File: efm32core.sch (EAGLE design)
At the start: 57 parts, among them U2 HM-10, U3 USD-SOCKETNEW, X1 48.0MHz, Y1 32.768kHz

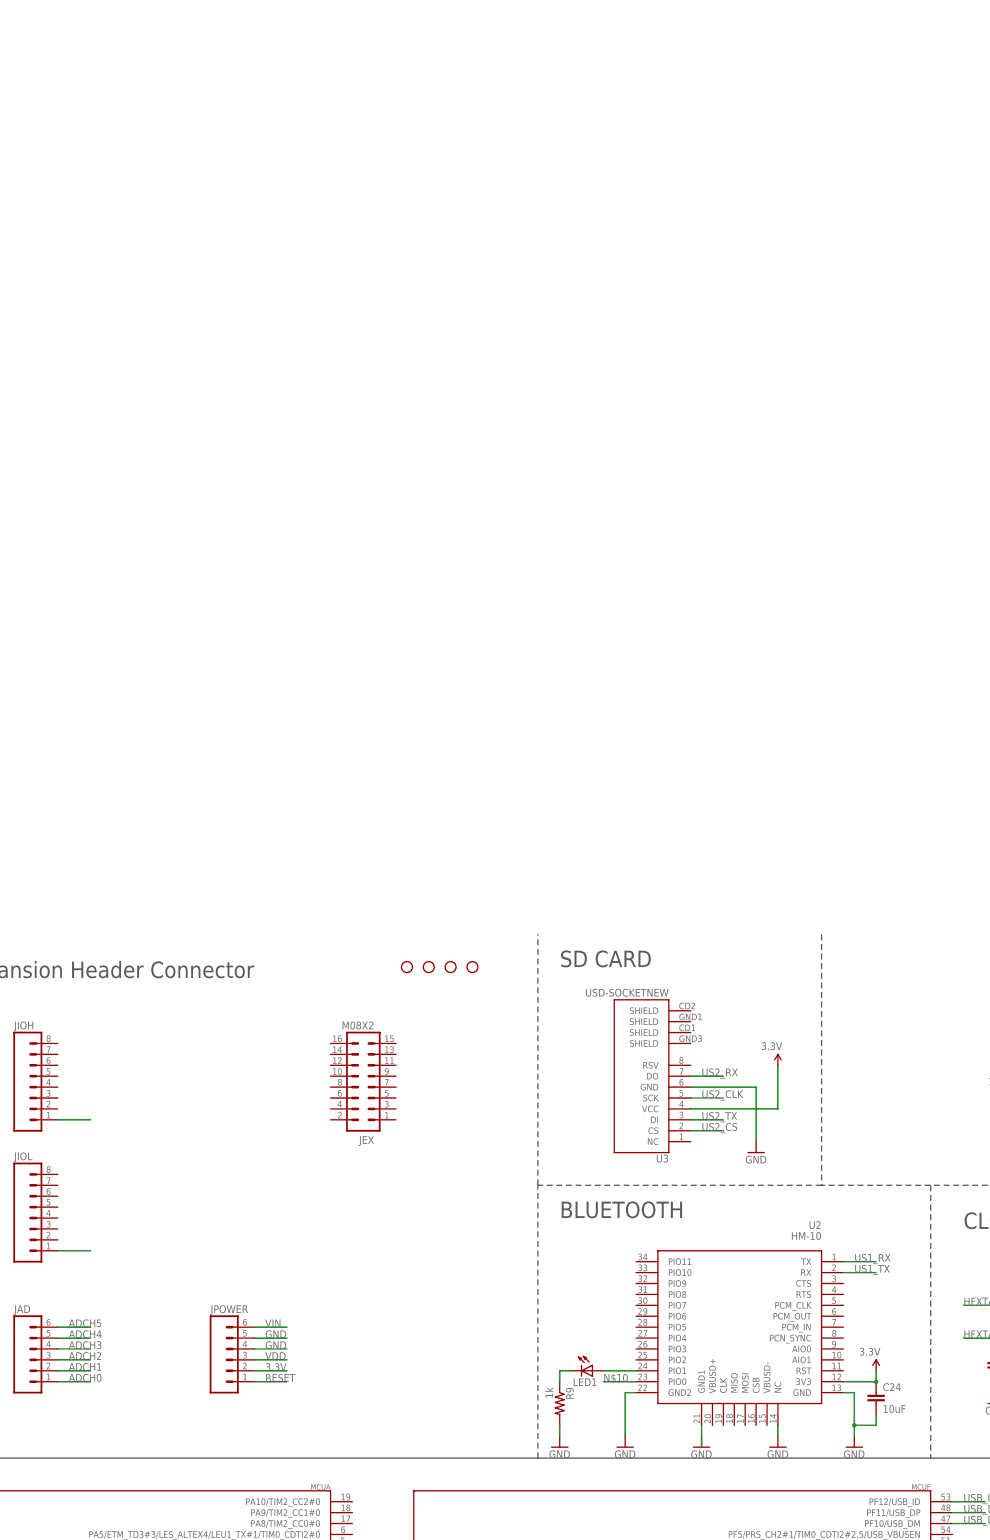
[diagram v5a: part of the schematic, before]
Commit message: update bluetooth and add co mcu
1. use a smaller footprint ble module
2. add a low power co cpu
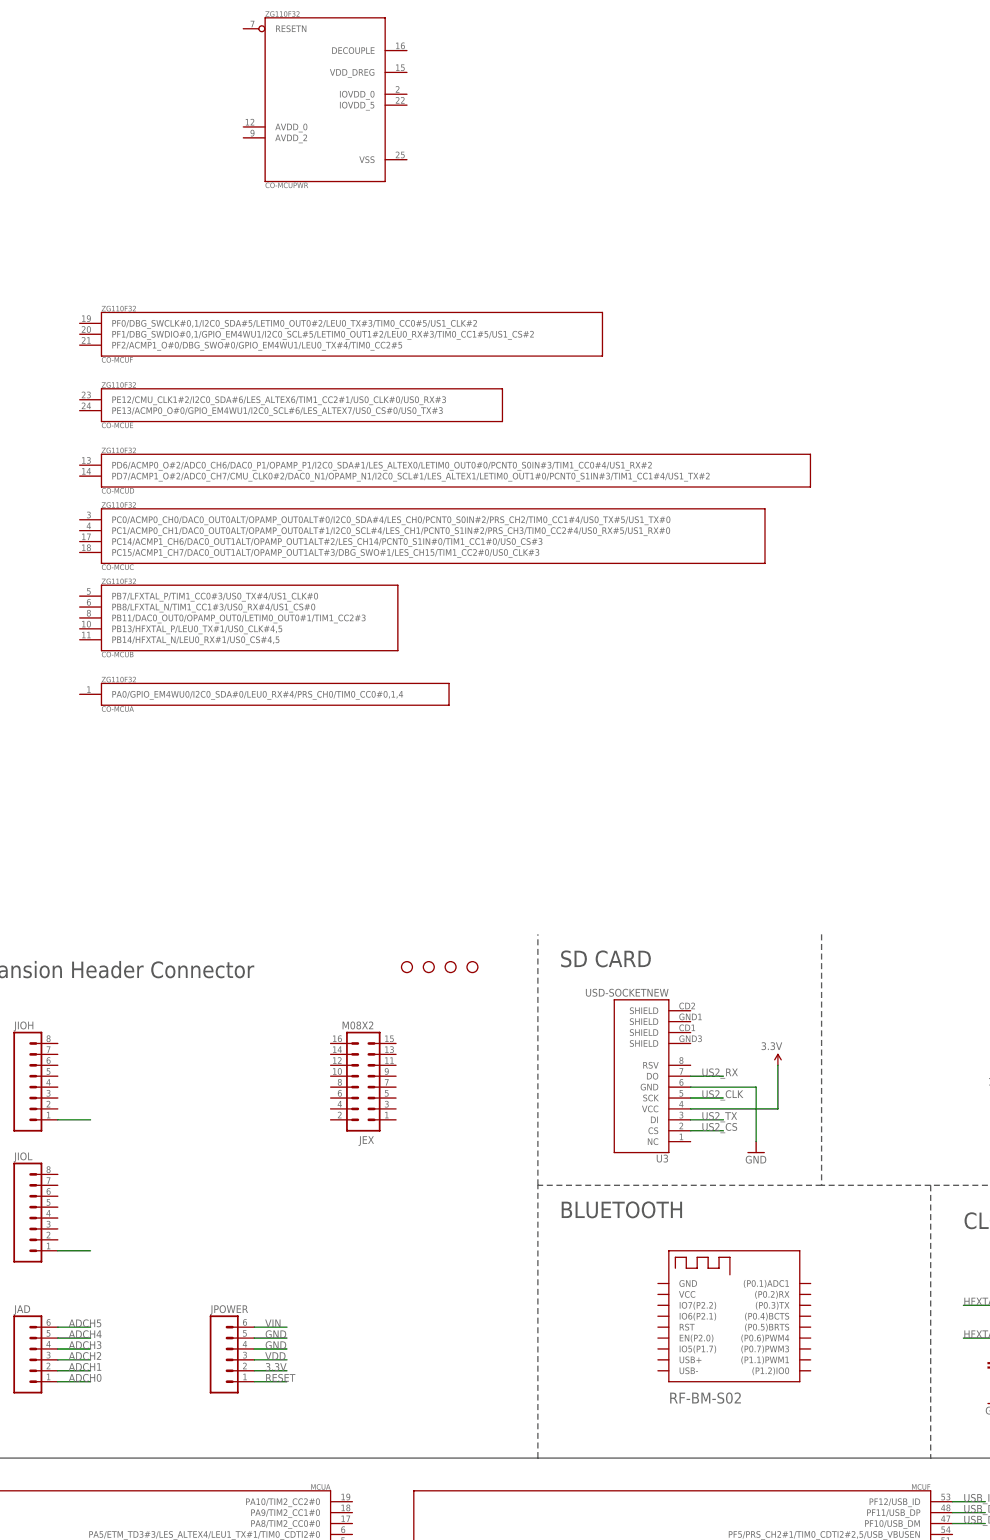
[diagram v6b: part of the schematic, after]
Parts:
- removed C24: 10uF, SparkFun-Capacitors:10UF-6.3V-20%(1206)
- removed LED1: (no value), adafruit:LEDCHIPLED_0603
- removed R9: 1k, SparkFun-Resistors:100OHM1/10W1%(0603)
- removed U2: HM-10, SerialPortBluetooth:HC_05
- added BM-S02: RF-BM-S02, szrfstar:RF-BM-S02
- added CO-MCU: ZG110F32, EnergyMicro:EFM32TG110F32
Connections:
- removed net N$10: U2.PIO0
- removed net N$16: U2.GND1
- removed net N$2: LED1.A, U2.PIO1
- removed net N$5: LED1.C, R9.1
- net 3.3V: no longer C24.1, U2.3V3
- net GND: no longer C24.2, R9.2, U2.GND, U2.GND2, U2.NC
- net US1_RX: no longer U2.TX
- net US1_TX: no longer U2.RX
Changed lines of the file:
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@@
 <part name="GND14" library="SparkFun-Aesthetics" deviceset="GND" device=""/>
 <part name="Y1" library="SparkFun-FreqCtrl" deviceset="CRYSTAL" device="5X1.5" value="32.768kHz"/>
-<part name="U2" library="SerialPortBluetooth" deviceset="HC_05" device="" value="HM-10"/>
 <part name="U3" library="SparkFun-Connectors" deviceset="USD-SOCKET" device="NEW"/>
 <part name="GND15" library="SparkFun-Aesthetics" deviceset="GND" device=""/>
@@
 <part name="GND17" library="SparkFun-Aesthetics" deviceset="GND" device=""/>
 <part name="C23" library="SparkFun-Capacitors" deviceset="10NF/10000PF-50V-10%(0603)" device="" value="10nF"/>
-<part name="C24" library="SparkFun-Capacitors" deviceset="10UF-6.3V-20%(1206)" device="" value="10uF"/>
-<part name="GND18" library="SparkFun-Aesthetics" deviceset="GND" device=""/>
-<part name="3.3V7" library="SparkFun-Aesthetics" deviceset="3.3V" device=""/>
-<part name="GND19" library="SparkFun-Aesthetics" deviceset="GND" device=""/>
-<part name="GND20" library="SparkFun-Aesthetics" deviceset="GND" device=""/>
-<part name="GND21" library="SparkFun-Aesthetics" deviceset="GND" device=""/>
-<part name="R9" library="SparkFun-Resistors" deviceset="100OHM1/10W1%(0603)" device="" value="1k"/>
-<part name="LED1" library="adafruit" deviceset="LED" device="CHIPLED_0603"/>
-<part name="GND22" library="SparkFun-Aesthetics" deviceset="GND" device=""/>
+<part name="BM-S02" library="szrfstar" deviceset="RF-BM-S02" device=""/>
+<part name="FRAME2" library="SparkFun-Aesthetics" deviceset="FRAME-A3" device=""/>
+<part name="CO-MCU" library="EnergyMicro" deviceset="EFM32TG110F32" device="" value="ZG110F32"/>
 </parts>
 <sheets>
@@
 <instance part="GND14" gate="1" x="292.1" y="147.32"/>
 <instance part="Y1" gate="G$1" x="284.48" y="162.56" rot="R180"/>
-<instance part="U2" gate="G$1" x="210.82" y="182.88" rot="MR0"/>
 <instance part="U3" gate="G$1" x="172.72" y="220.98" rot="R180"/>
 <instance part="GND15" gate="1" x="195.58" y="205.74"/>
@@
 <instance part="GND17" gate="1" x="363.22" y="210.82"/>
 <instance part="C23" gate="G$1" x="358.14" y="182.88"/>
-<instance part="C24" gate="G$1" x="223.52" y="147.32"/>
-<instance part="GND18" gate="1" x="218.44" y="137.16"/>
-<instance part="3.3V7" gate="G$1" x="223.52" y="154.94" rot="MR0"/>
-<instance part="GND19" gate="1" x="200.66" y="137.16"/>
-<instance part="GND20" gate="1" x="165.1" y="137.16"/>
-<instance part="GND21" gate="1" x="182.88" y="137.16"/>
-<instance part="R9" gate="G$1" x="149.86" y="147.32" rot="R270"/>
-<instance part="LED1" gate="G$1" x="157.48" y="154.94" rot="R270"/>
-<instance part="GND22" gate="1" x="149.86" y="137.16"/>
+<instance part="BM-S02" gate="G$1" x="175.26" y="152.4"/>
+<instance part="FRAME2" gate="G$1" x="0" y="271.78"/>
+<instance part="CO-MCU" gate="A" x="38.1" y="314.96"/>
+<instance part="CO-MCU" gate="B" x="38.1" y="337.82"/>
+<instance part="CO-MCU" gate="C" x="38.1" y="355.6"/>
+<instance part="CO-MCU" gate="D" x="38.1" y="368.3"/>
+<instance part="CO-MCU" gate="E" x="38.1" y="383.54"/>
+<instance part="CO-MCU" gate="F" x="38.1" y="401.32"/>
+<instance part="CO-MCU" gate="PWR" x="76.2" y="469.9"/>
 </instances>
 <busses>
@@
 <junction x="327.66" y="248.92"/>
 </segment>
-<segment>
-<pinref part="U2" gate="G$1" pin="3V3"/>
-<wire x1="215.9" y1="152.4" x2="223.52" y2="152.4" width="0.1524" layer="91"/>
-<pinref part="C24" gate="G$1" pin="1"/>
-<pinref part="3.3V7" gate="G$1" pin="3.3V"/>
-<wire x1="223.52" y1="154.94" x2="223.52" y2="152.4" width="0.1524" layer="91"/>
-<junction x="223.52" y="152.4"/>
-</segment>
 </net>
 <net name="VDD" class="0">
@@
 <wire x1="363.22" y1="213.36" x2="363.22" y2="215.9" width="0.1524" layer="91"/>
 </segment>
-<segment>
-<pinref part="U2" gate="G$1" pin="GND"/>
-<wire x1="215.9" y1="149.86" x2="218.44" y2="149.86" width="0.1524" layer="91"/>
-<wire x1="218.44" y1="149.86" x2="218.44" y2="142.24" width="0.1524" layer="91"/>
-<pinref part="GND18" gate="1" pin="GND"/>
-<pinref part="C24" gate="G$1" pin="2"/>
-<wire x1="218.44" y1="142.24" x2="218.44" y2="139.7" width="0.1524" layer="91"/>
-<wire x1="223.52" y1="144.78" x2="223.52" y2="142.24" width="0.1524" layer="91"/>
-<wire x1="223.52" y1="142.24" x2="218.44" y2="142.24" width="0.1524" layer="91"/>
-<junction x="218.44" y="142.24"/>
-</segment>
-<segment>
-<pinref part="U2" gate="G$1" pin="GND2"/>
-<wire x1="167.64" y1="149.86" x2="165.1" y2="149.86" width="0.1524" layer="91"/>
-<pinref part="GND20" gate="1" pin="GND"/>
-<wire x1="165.1" y1="149.86" x2="165.1" y2="139.7" width="0.1524" layer="91"/>
-</segment>
-<segment>
-<pinref part="U2" gate="G$1" pin="NC"/>
-<pinref part="GND19" gate="1" pin="GND"/>
-<wire x1="200.66" y1="142.24" x2="200.66" y2="139.7" width="0.1524" layer="91"/>
-</segment>
-<segment>
-<pinref part="R9" gate="G$1" pin="2"/>
-<pinref part="GND22" gate="1" pin="GND"/>
-<wire x1="149.86" y1="142.24" x2="149.86" y2="139.7" width="0.1524" layer="91"/>
-</segment>
 </net>
 <net name="5V" class="0">
@@
 <label x="200.66" y="7.62" size="1.778" layer="95"/>
 </segment>
-<segment>
-<pinref part="U2" gate="G$1" pin="RX"/>
-<wire x1="215.9" y1="177.8" x2="223.52" y2="177.8" width="0.1524" layer="91"/>
-<label x="218.44" y="177.8" size="1.778" layer="95"/>
-</segment>
 </net>
 <net name="US1_RX" class="0">
@@
 <wire x1="198.12" y1="10.16" x2="205.74" y2="10.16" width="0.1524" layer="91"/>
 <label x="200.66" y="10.16" size="1.778" layer="95"/>
-</segment>
-<segment>
-<pinref part="U2" gate="G$1" pin="TX"/>
-<wire x1="215.9" y1="180.34" x2="223.52" y2="180.34" width="0.1524" layer="91"/>
-<label x="218.44" y="180.34" size="1.778" layer="95"/>
 </segment>
 </net>
@@
 </segment>
 </net>
-<net name="N$16" class="0">
-<segment>
-<pinref part="U2" gate="G$1" pin="GND1"/>
-<wire x1="182.88" y1="142.24" x2="182.88" y2="137.16" width="0.1524" layer="91"/>
-</segment>
-</net>
-<net name="N$2" class="0">
-<segment>
-<pinref part="U2" gate="G$1" pin="PIO1"/>
-<pinref part="LED1" gate="G$1" pin="A"/>
-<wire x1="167.64" y1="154.94" x2="160.02" y2="154.94" width="0.1524" layer="91"/>
-</segment>
-</net>
-<net name="N$5" class="0">
-<segment>
-<pinref part="LED1" gate="G$1" pin="C"/>
-<wire x1="152.4" y1="154.94" x2="149.86" y2="154.94" width="0.1524" layer="91"/>
-<pinref part="R9" gate="G$1" pin="1"/>
-<wire x1="149.86" y1="154.94" x2="149.86" y2="152.4" width="0.1524" layer="91"/>
-</segment>
-</net>
-<net name="N$10" class="0">
-<segment>
-<pinref part="U2" gate="G$1" pin="PIO0"/>
-<wire x1="167.64" y1="152.4" x2="160.02" y2="152.4" width="0.1524" layer="91"/>
-<label x="160.02" y="152.4" size="1.778" layer="95"/>
-</segment>
-</net>

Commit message: temporary update
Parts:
- added C24: 10nF, SparkFun-Capacitors:10NF/10000PF-50V-10%(0603)
- added C25: 47uF, SparkFun-Capacitors:10NF/10000PF-50V-10%(0603)
- added LED1, LED2: (no value), SparkFun-LED:LED0603
- added Q1: MMBT5088, SparkFun-DiscreteSemi:TRANSISTOR_NPNMMBT5088
- added R10, R11: 470, SparkFun-Resistors:100-1%
- added R12: 4.7k, SparkFun-Resistors:100-1%
- added R9: 1k, SparkFun-Resistors:100-1%
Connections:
- new net N$10: R9.1
- new net N$11: LED1.C, R9.2
- new net N$16: BM-S02.IO7(P2.2)
- new net N$17: BM-S02.IO6(P2.1)
- new net N$18: BM-S02.VCC, C24.1, C25.1, Q1.E
- new net N$19: Q1.B, R11.2
- new net N$2: R10.1
- new net N$20: R11.1
- new net N$22: BM-S02.RST, R12.2
- new net N$23: BM-S02.EN(P2.0)
- new net N$24: BM-S02.(P0.5)BRTS
- new net N$25: BM-S02.(P0.4)BCTS
- new net N$26: BM-S02.(P1.2)IO0
- new net N$27: BM-S02.(P0.2)RX
- new net N$28: BM-S02.(P0.3)TX
- new net N$5: LED2.A, R10.2
- net 3.3V: now also LED1.A, Q1.C, R12.1
- net GND: now also BM-S02.GND, C24.2, C25.2, LED2.C

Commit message: update bluetooth module, replace with BLE112
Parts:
- removed BM-S02: RF-BM-S02, szrfstar:RF-BM-S02
- removed CO-MCU: ZG110F32, EnergyMicro:EFM32TG110F32
- removed LED1, LED2: (no value), SparkFun-LED:LED0603
- removed R12: 4.7k, SparkFun-Resistors:100-1%
- added BLE112-A: SF-BLUEGIGA_BLE112-A-VISUAL, BLE112-Breakout-Board-v2.1:SF-BLUEGIGA_BLE112-A-VISUAL
- added C26: 0.47uF, SparkFun-Capacitors:10NF/10000PF-50V-10%(0603)
- added JP1, JP2: JUMPER-3SMD, SparkFun-Passives:JUMPER-3SMD
- added LOGO1: OSHW-LOGOL, SparkFun-Aesthetics:OSHW-LOGOL
- added SJ1, SJ2: (no value), BLE112-Breakout-Board-v2.1:JUMPER_SJ
- C24: value 10nF -> 0.47uF
- C25: value 47uF -> 0.47uF
- R10: value 470 -> 1.5k
- R9: value 1k -> 10k
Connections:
- removed net N$10: R9.1
- removed net N$11: LED1.C, R9.2
- removed net N$16: BM-S02.IO7(P2.2)
- removed net N$17: BM-S02.IO6(P2.1)
- removed net N$18: BM-S02.VCC, C24.1, C25.1, Q1.E
- removed net N$2: R10.1
- removed net N$22: BM-S02.RST, R12.2
- removed net N$23: BM-S02.EN(P2.0)
- removed net N$24: BM-S02.(P0.5)BRTS
- removed net N$25: BM-S02.(P0.4)BCTS
- removed net N$26: BM-S02.(P1.2)IO0
- removed net N$27: BM-S02.(P0.2)RX
- removed net N$28: BM-S02.(P0.3)TX
- removed net N$5: LED2.A, R10.2
- new net 3.3V-BLE: BLE112-A.AVDD, BLE112-A.AVDD@2, BLE112-A.DVDD, BLE112-A.VDD_USB, C24.1, C25.1, C26.1, Q1.E, R9.2
- new net BLE-P1_0: BLE112-A.P1_0, R10.1
- new net BLE-RST: BLE112-A.RESET, R9.1, SJ1.1
- new net BLE-USB+: BLE112-A.USB+, JP2.1, R10.2
- new net BLE-USB-: BLE112-A.USB-, JP1.1
- new net M_USB_DM: JP1.3, MCUF.PF10/USB_DM
- new net M_USB_DP: JP2.3, MCUF.PF11/USB_DP
- new net M_USB_ID: MCUF.PF12/USB_ID, SJ2.1
- net 3.3V: no longer LED1.A, R12.1
- net GND: now also BLE112-A.GND, BLE112-A.GND@2, BLE112-A.GND@3, BLE112-A.GND@4, C26.2, SJ1.2; no longer BM-S02.GND, LED2.C
- net USB_DM: now also JP1.2; no longer MCUF.PF10/USB_DM
- net USB_DP: now also JP2.2; no longer MCUF.PF11/USB_DP
- net USB_ID: now also SJ2.2; no longer MCUF.PF12/USB_ID
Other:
- note added: "C24, C25, C26 are placed near two AVDDs, VDD_USB and DVDD separately."
- note added: "JUMPER"
- moved on the sheet: C24, C25, C4, JEX, JPOWER, Q1, R10, R11, R9, U3
